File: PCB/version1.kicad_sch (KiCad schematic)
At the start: 21 parts, among them J1 USB_C_Receptacle_USB2.0_16P, SW1 SW_SPST, SW2 SW_SPST, SW3 RotaryEncoder_Switch, U1 STM32F072CBTx, U2 XC6206PxxxMR

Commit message: PCB and gerbers with BOM
Added KiCad Project files along with gerbers for production and Bill of Materials
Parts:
- SW1, SW2: footprint Button_Switch_SMD:SW_SPST_TL3342 -> Button_Switch_SMD:SW_SPST_TS-1088-xR020
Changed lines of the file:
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@@
 			)
 		)
-		(property "Footprint" "Button_Switch_SMD:SW_SPST_TL3342"
+		(property "Footprint" "Button_Switch_SMD:SW_SPST_TS-1088-xR020"
 			(at 224.79 115.57 0)
 			(hide yes)
@@
 			)
 		)
-		(property "Footprint" "Button_Switch_SMD:SW_SPST_TL3342"
+		(property "Footprint" "Button_Switch_SMD:SW_SPST_TS-1088-xR020"
 			(at 264.16 115.57 0)
 			(hide yes)

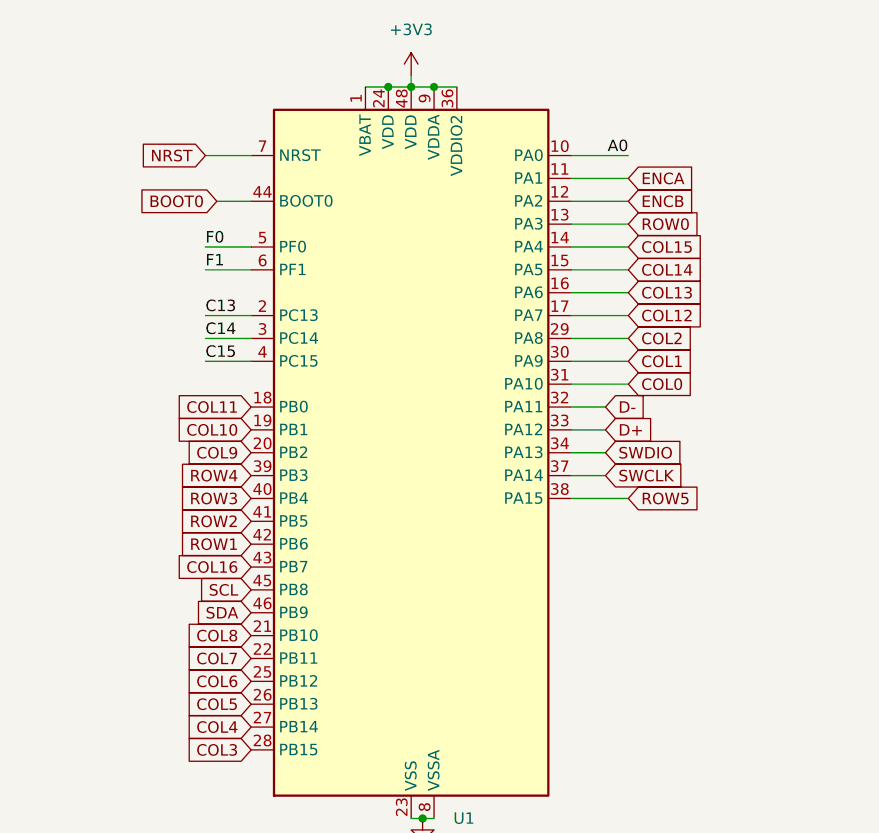
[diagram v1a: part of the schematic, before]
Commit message: Updated PCB, gerbers and added STEP files to production folder
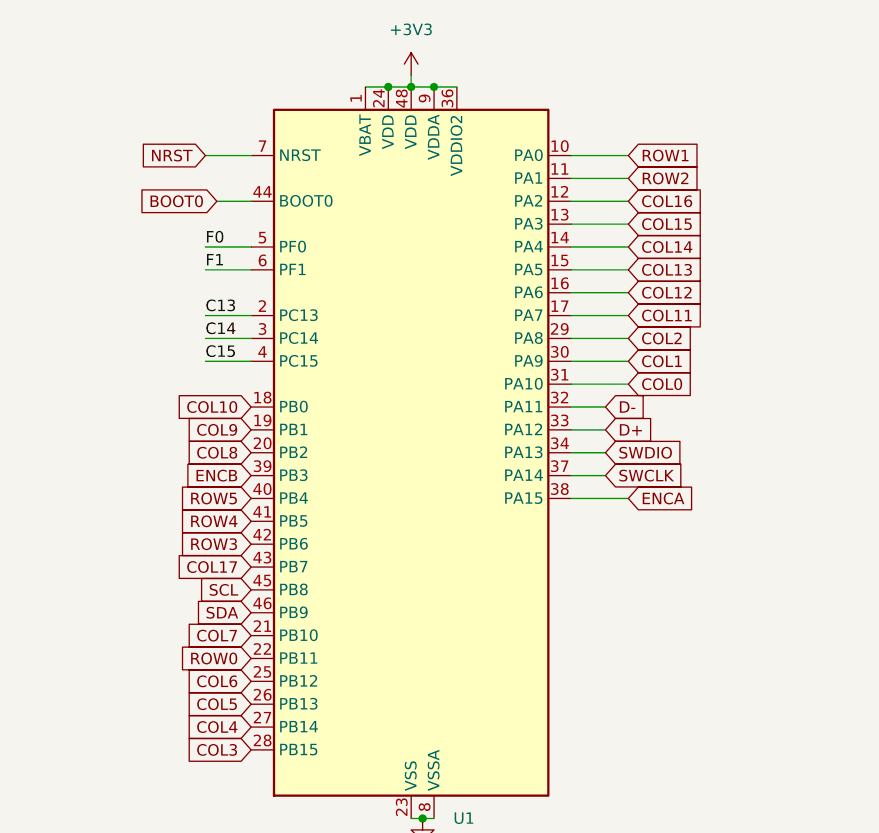
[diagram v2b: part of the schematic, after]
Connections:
- net A0 is gone; now on net ROW1: U1.10 (PA0)
- net COL10: now also U1.18 (PB0); no longer U1.19 (PB1)
- net COL11: now also U1.17 (PA7); no longer U1.18 (PB0)
- net COL12: now also U1.16 (PA6); no longer U1.17 (PA7)
- net COL13: now also U1.15 (PA5); no longer U1.16 (PA6)
- net COL14: now also U1.14 (PA4); no longer U1.15 (PA5)
- net COL15: now also U1.13 (PA3); no longer U1.14 (PA4)
- net COL16: now also U1.12 (PA2); no longer U1.43 (PB7)
- net COL7: now also U1.21 (PB10); no longer U1.22 (PB11)
- net COL8: now also U1.20 (PB2); no longer U1.21 (PB10)
- net COL9: now also U1.19 (PB1); no longer U1.20 (PB2)
- net ENCA: now also U1.38 (PA15); no longer U1.11 (PA1)
- net ENCB: now also U1.39 (PB3); no longer U1.12 (PA2)
- net ROW0: now also U1.22 (PB11); no longer U1.13 (PA3)
- net ROW1: no longer U1.42 (PB6)
- net ROW2: now also U1.11 (PA1); no longer U1.41 (PB5)
- net ROW3: now also U1.42 (PB6); no longer U1.40 (PB4)
- net ROW4: now also U1.41 (PB5); no longer U1.39 (PB3)
- net ROW5: now also U1.40 (PB4); no longer U1.38 (PA15)
- new net COL17: U1.43 (PB7)

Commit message: Updated schematic
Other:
- note added: "BOOT0"
- note added: "Decoupling Capacitors"
- note added: "MCU"
- note added: "NRST"
- note added: "Rotary Encoder"
- note added: "USB-C"
- moved on the sheet: J1, R1, R2, SW3, U1

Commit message: Updated PCB files
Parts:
- added J2: Conn_01x04_Pin, Connector_PinHeader_2.54mm:PinHeader_1x04_P2.54mm_Horizontal, symbol Connector:Conn_01x04_Pin
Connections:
- net +3V3: now also J2.1 (Pin_1)
- net GND: now also J2.4 (Pin_4)
- net SWCLK: now also J2.3 (Pin_3)
- net SWDIO: now also J2.2 (Pin_2)

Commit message: minor changes
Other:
- note added: "Debug"
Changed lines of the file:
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@@
+	)
+	(rectangle
+		(start 175.895 140.97)
+		(end 204.47 164.465)
+		(stroke
+			(width 0)
+			(type default)
+		)
+		(fill
+			(type none)
+		)
 	)
 	(rectangle
@@
 		(effects
 			(font
+				(size 2.54 2.54)
+				(thickness 0.762)
+				(bold yes)
+				(color 0 255 255 1)
+			)
+		)
+	)
+	(text "Debug\n"
+		(exclude_from_sim no)
+		(at 191.262 138.938 0)
+		(effects
+			(font
